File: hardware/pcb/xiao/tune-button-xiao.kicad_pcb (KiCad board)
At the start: 2 copper layers, 46 x 67 mm, 18 parts, among them J1 XIAO left, J2 XIAO right, J3 LiPo, J4 to XIAO BAT, SW1 MX switch, SW2 MX switch, SW3 MX switch, SW4 MX switch

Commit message: pcb: fixes from the sixth DFM audit
- Back-side SMD parts (the hand-soldered LEDs) get a rule area between
  their pads: no tracks, vias or pour there. The re-route had threaded
  VBAT between D3's pads, beside its GND pad, where a solder bridge would
  short the battery.
- Stitching now aims for two GND vias at least 2 mm apart in every pour
  island, not one. U3's ground pad (the charger's heat path) sits on a
  30 mm2 island with three vias; it had been on a 10 mm2 one with one.
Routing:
- net LED: track 26.9 -> 37.9 mm, vias 0 -> 1
- net K3: track 67.3 -> 61.2 mm, vias 0 -> 1
- net VBAT: track 17.3 -> 21.4 mm
- net VBAT_SENSE: track 25.3 -> 28.0 mm
- net K4: track 55.4 -> 57.1 mm
- net K1: track 23.1 -> 22.2 mm
- net GND: track 7.62 -> 7.80 mm, vias 200 -> 206

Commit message: pcb: round-8 audit suggestions
- J1 keepout starts at the shell's metal floor (0.7 mm past the pad tips);
  the D- stubs stop short of it.
- VBUS pad pairs joined through their own power vias and a back-side link,
  so VBUS no longer runs along the GND pads and shell legs.
- D+ link 0.5 mm clear of the A7/B7 tips.
- U2 (ESD) gets its own GND via off its ground pin; U2 moves 0.5 mm up for it.
- Stitcher gives a via-less GND island one wherever a via fits in both pours.
- No vias within 0.6 mm of back-side hand-soldered pads, or under part labels
  and the JLC mark.
- route.py drops zero-length segments with the duplicates.
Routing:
- net LED: track 37.9 -> 26.9 mm, vias 1 -> 0
- net K2: track 34.0 -> 27.5 mm
- net VBAT: track 21.4 -> 17.2 mm
- net VBAT_SENSE: track 28.0 -> 24.7 mm
- net K3: track 61.2 -> 63.2 mm, vias 1 -> 0
- net K4: track 57.1 -> 55.6 mm
- net GND: track 7.80 -> 6.47 mm, vias 206 -> 196
- net K1: track 22.2 -> 23.1 mm

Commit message: pcb: round-9 audit fixes; freeze the routing
Round 9 suggestions: keep back tracks off the logo, vias out from under all
front text, standard VBUS vias 0.5 mm out, drop sub-10 um segments, space
stitching vias by copper and anchor islands to any GND via, and reject
autoroute attempts that drop back-plane pour or run another net within
0.4 mm of a switch pin.

Freerouting lays the board out afresh on every run, so each review was of a
new layout. route.py now replays a reviewed routing from <board>/routing.json;
--reroute autoroutes, --freeze records. The back-part via margin is 0.25 mm
(vias are tented; at 0.6 mm the router ran out of room). XIAO: K3 moved off
SW1 pin 1; C3: two stitching vias removed from under the SW3/SW4 labels.
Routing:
- net K2: track 27.5 -> 34.0 mm
- net K3: track 63.2 -> 58.3 mm
- net K4: track 55.6 -> 59.8 mm
- net LED: track 26.9 -> 29.5 mm, vias 0 -> 1
- net GND: track 6.47 -> 6.16 mm, vias 196 -> 202

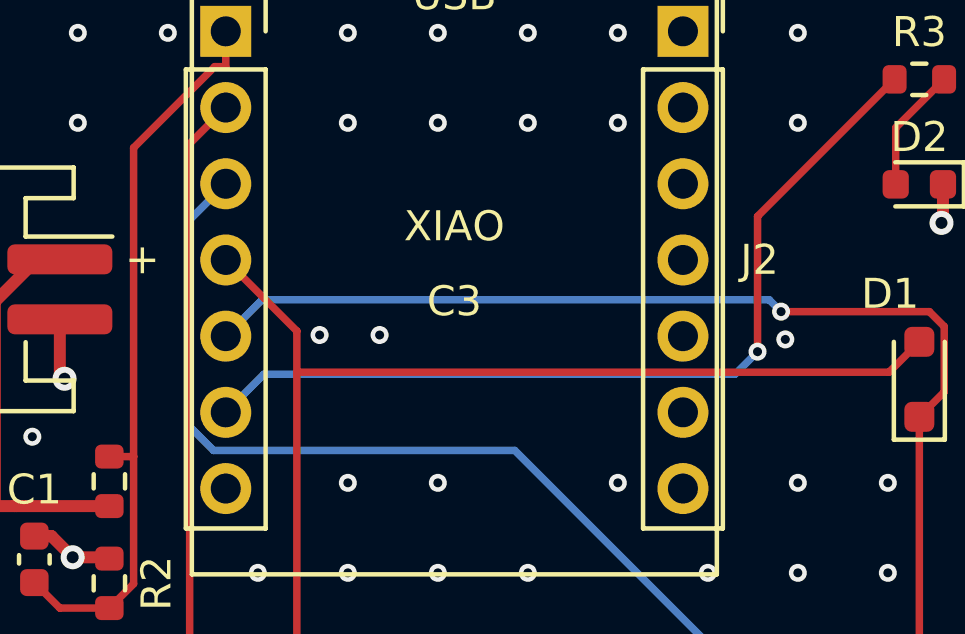
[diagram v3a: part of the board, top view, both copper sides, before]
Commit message: pcb: round-10 audit fixes
- The pin-gap check covers every hand-soldered through-hole pin (no LCSC
  number): switches on both layers, headers and sockets on the solder side,
  0.4 mm, or 0.29 mm for a track crossing a header row between two pins.
- Replaying routing.json runs the pin-gap and lost-pour checks too, so a
  hand edit has to meet them.
- XIAO: K2 moved 0.4 mm clear of J1 pins 4-7; K4 centred between J2 pins 4
  and 5. C3: K4 moved 0.4 mm clear of TP1.
- C3: second GND vias on the strip beside D+ (R2) and on the R5 island.
- Segments under 0.02 mm are dropped; two such were removed.
- README: nylon washers or standoffs at the C3's mounting holes (H3 has
  tracks within 2 mm).
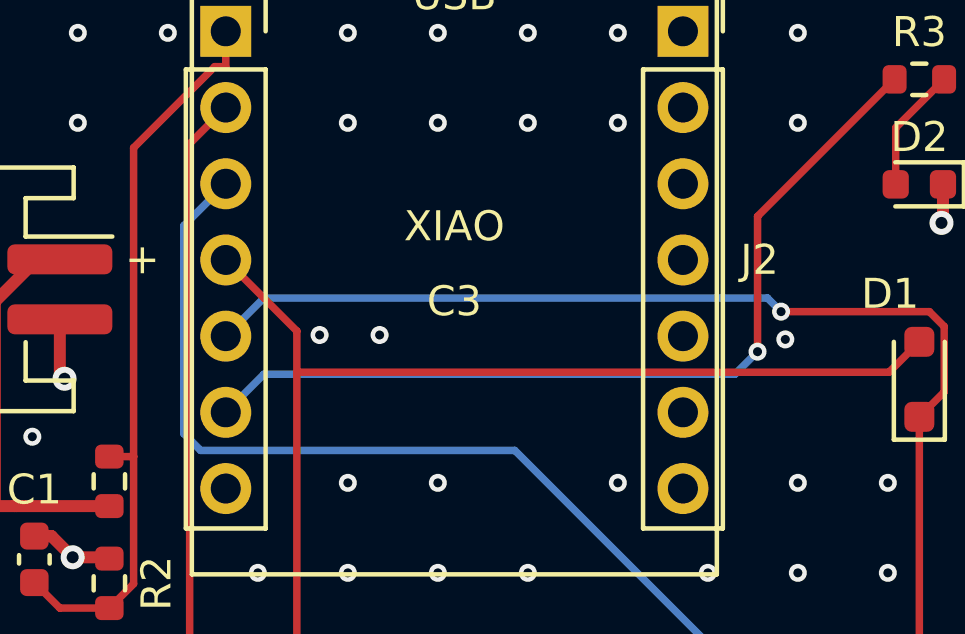
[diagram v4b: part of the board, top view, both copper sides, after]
